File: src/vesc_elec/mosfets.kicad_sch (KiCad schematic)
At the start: 44 parts, among them Q1 NCEP60T20, Q2 NCEP60T20, Q3 NCEP60T20, Q4 NCEP60T20, Q5 NCEP60T20, Q6 NCEP60T20

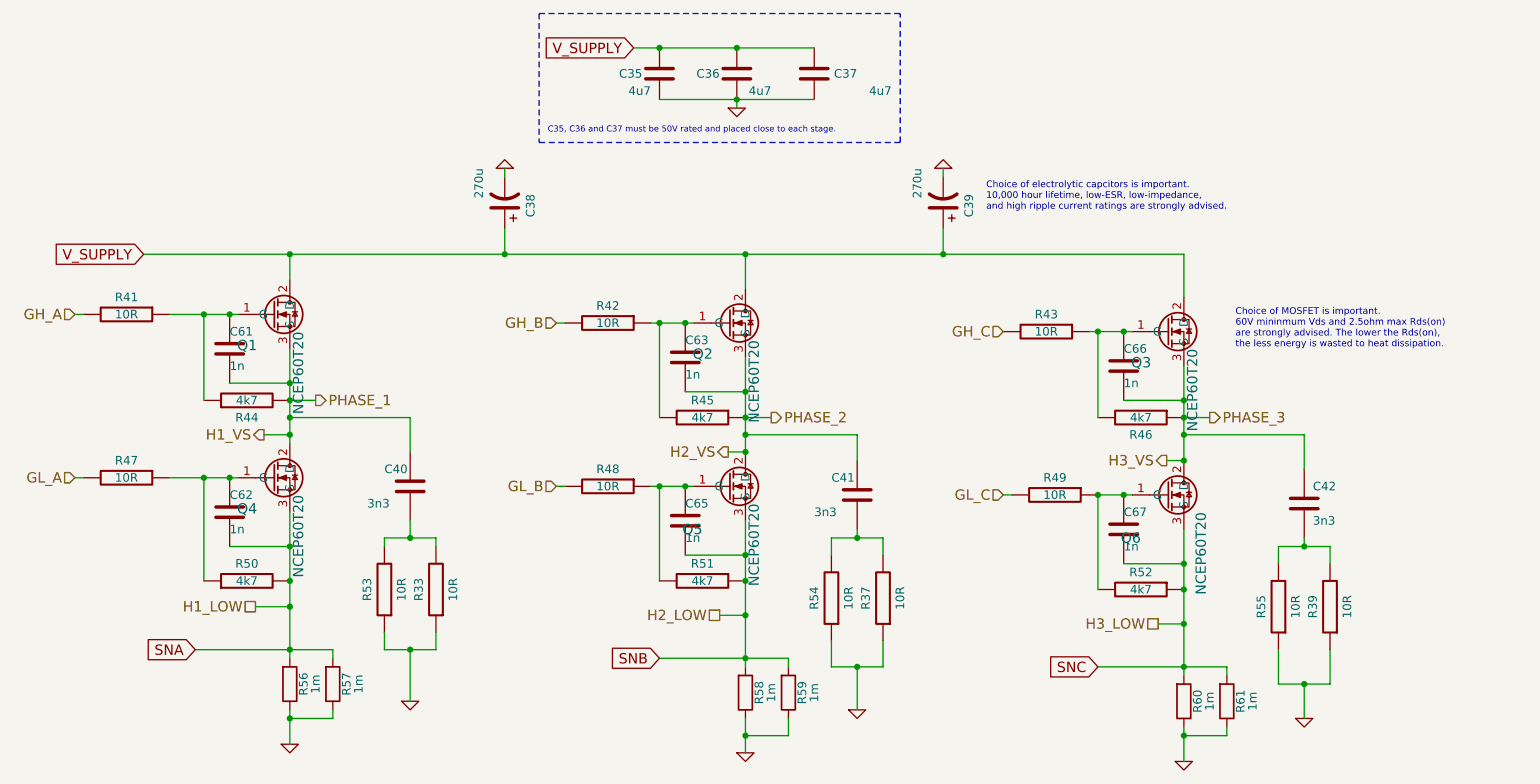
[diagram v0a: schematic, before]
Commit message: [VESC] Swap phase A and C MOSFET labels (#123)
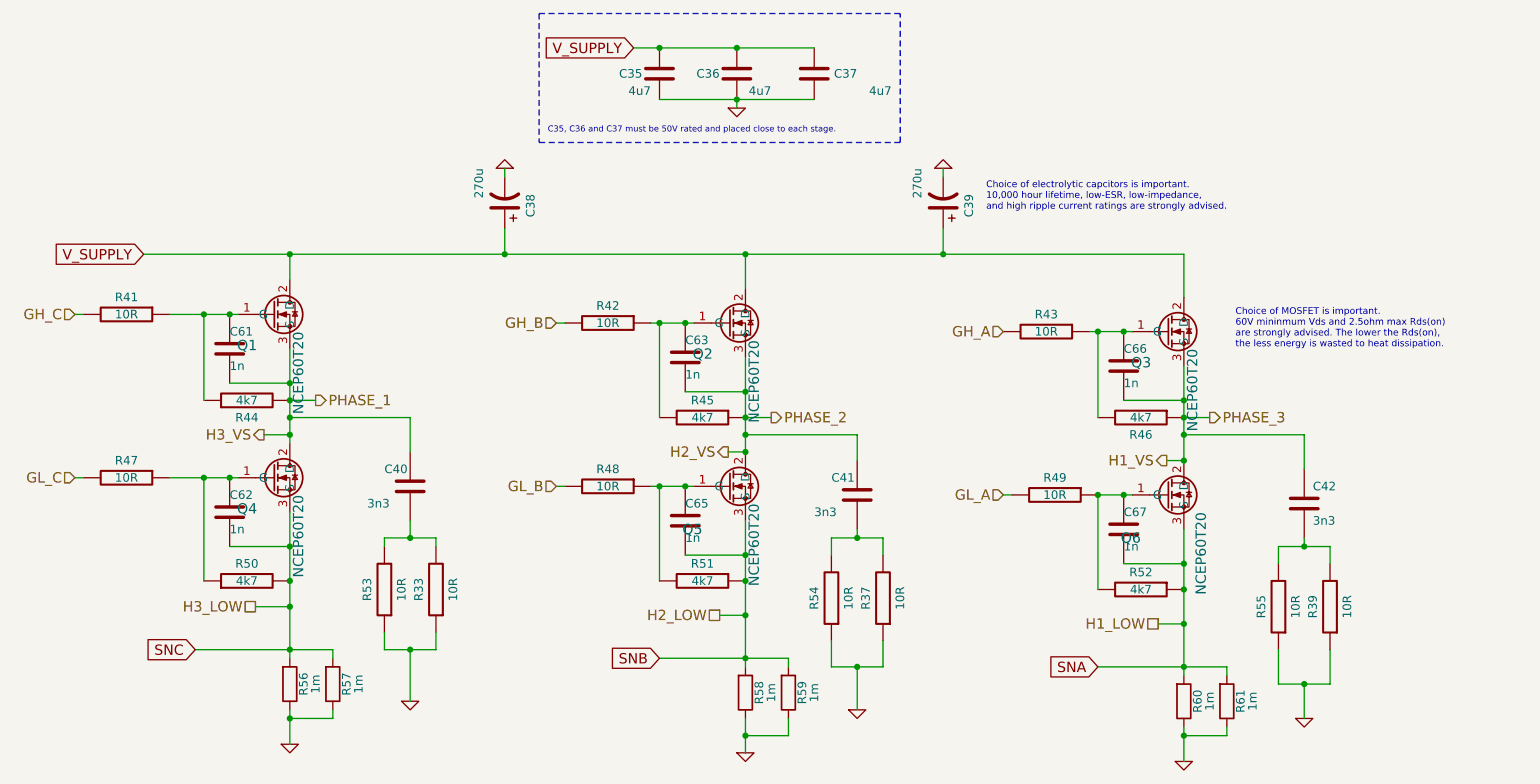
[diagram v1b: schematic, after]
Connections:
- net GH_A: now also R43.2; no longer R41.2
- net GH_C: now also R41.2; no longer R43.2
- net GL_A: now also R49.2; no longer R47.2
- net GL_C: now also R47.2; no longer R49.2
- net H1_VS: now also C42.1, C66.2, Q3.3 (S), Q6.2 (D), Q6.4 (Heatsink), R46.1; no longer C40.1, C61.2, Q1.3 (S), Q4.2 (D), Q4.4 (Heatsink), R44.2
- net H3_VS: now also C40.1, C61.2, Q1.3 (S), Q4.2 (D), Q4.4 (Heatsink), R44.2; no longer C42.1, C66.2, Q3.3 (S), Q6.2 (D), Q6.4 (Heatsink), R46.1
- net SNA: now also C67.2, Q6.3 (S), R52.1, R60.2, R61.2; no longer C62.2, Q4.3 (S), R50.2, R56.2, R57.2
- net SNC: now also C62.2, Q4.3 (S), R50.2, R56.2, R57.2; no longer C67.2, Q6.3 (S), R52.1, R60.2, R61.2
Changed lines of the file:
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@@
+		)
+	)
+	(global_label "SNC"
+		(shape input)
+		(at 81.28 129.54 180)
+		(effects
+			(font
+				(size 1.524 1.524)
+			)
+			(justify right)
+		)
+		(property "Intersheetrefs" "${INTERSHEET_REFS}"
+			(at 81.28 129.54 0)
+			(effects
+				(font
+					(size 1.27 1.27)
+				)
+				(hide yes)
+			)
+		)
+	)
+	(global_label "SNB"
+		(shape input)
+		(at 149.86 130.81 180)
+		(effects
+			(font
+				(size 1.524 1.524)
+			)
+			(justify right)
+		)
+		(property "Intersheetrefs" "${INTERSHEET_REFS}"
+			(at 149.86 130.81 0)
+			(effects
+				(font
+					(size 1.27 1.27)
+				)
+				(hide yes)
+			)
+		)
+	)
+	(global_label "V_SUPPLY"
+		(shape input)
+		(at 146.05 40.64 180)
+		(effects
+			(font
+				(size 1.524 1.524)
+			)
+			(justify right)
+		)
+		(property "Intersheetrefs" "${INTERSHEET_REFS}"
+			(at 146.05 40.64 0)
+			(effects
+				(font
+					(size 1.27 1.27)
+				)
+				(hide yes)
+			)
 		)
 	)
 	(global_label "SNA"
 		(shape input)
-		(at 81.28 129.54 180)
-		(effects
-			(font
-				(size 1.524 1.524)
-			)
-			(justify right)
-		)
-		(property "Intersheetrefs" "${INTERSHEET_REFS}"
-			(at 81.28 129.54 0)
-			(effects
-				(font
-					(size 1.27 1.27)
-				)
-				(hide yes)
-			)
-		)
-	)
-	(global_label "SNB"
-		(shape input)
-		(at 149.86 130.81 180)
-		(effects
-			(font
-				(size 1.524 1.524)
-			)
-			(justify right)
-		)
-		(property "Intersheetrefs" "${INTERSHEET_REFS}"
-			(at 149.86 130.81 0)
+		(at 214.63 132.08 180)
+		(effects
+			(font
+				(size 1.524 1.524)
+			)
+			(justify right)
+		)
+		(property "Intersheetrefs" "${INTERSHEET_REFS}"
+			(at 214.63 132.08 0)
 			(effects
 				(font
@@
 	(global_label "V_SUPPLY"
 		(shape input)
-		(at 146.05 40.64 180)
-		(effects
-			(font
-				(size 1.524 1.524)
-			)
-			(justify right)
-		)
-		(property "Intersheetrefs" "${INTERSHEET_REFS}"
-			(at 146.05 40.64 0)
-			(effects
-				(font
-					(size 1.27 1.27)
-				)
-				(hide yes)
-			)
-		)
-	)
-	(global_label "SNC"
-		(shape input)
-		(at 214.63 132.08 180)
-		(effects
-			(font
-				(size 1.524 1.524)
-			)
-			(justify right)
-		)
-		(property "Intersheetrefs" "${INTERSHEET_REFS}"
-			(at 214.63 132.08 0)
-			(effects
-				(font
-					(size 1.27 1.27)
-				)
-				(hide yes)
-			)
-		)
-	)
-	(global_label "V_SUPPLY"
-		(shape input)
 		(at 73.66 71.12 180)
 		(effects
@@
 			)
 			(justify left)
+		)
+	)
+	(hierarchical_label "H1_LOW"
+		(shape passive)
+		(at 223.52 125.73 180)
+		(effects
+			(font
+				(size 1.524 1.524)
+			)
+			(justify right)
+		)
+	)
+	(hierarchical_label "GH_C"
+		(shape input)
+		(at 63.5 80.01 180)
+		(effects
+			(font
+				(size 1.524 1.524)
+			)
+			(justify right)
+		)
+	)
+	(hierarchical_label "H2_VS"
+		(shape output)
+		(at 160.02 100.33 180)
+		(effects
+			(font
+				(size 1.524 1.524)
+			)
+			(justify right)
+		)
+	)
+	(hierarchical_label "GL_C"
+		(shape input)
+		(at 63.5 104.14 180)
+		(effects
+			(font
+				(size 1.524 1.524)
+			)
+			(justify right)
 		)
 	)
 	(hierarchical_label "H3_LOW"
 		(shape passive)
-		(at 223.52 125.73 180)
+		(at 90.17 123.19 180)
+		(effects
+			(font
+				(size 1.524 1.524)
+			)
+			(justify right)
+		)
+	)
+	(hierarchical_label "GH_B"
+		(shape input)
+		(at 134.62 81.28 180)
+		(effects
+			(font
+				(size 1.524 1.524)
+			)
+			(justify right)
+		)
+	)
+	(hierarchical_label "GL_A"
+		(shape input)
+		(at 200.66 106.68 180)
+		(effects
+			(font
+				(size 1.524 1.524)
+			)
+			(justify right)
+		)
+	)
+	(hierarchical_label "GL_B"
+		(shape input)
+		(at 134.62 105.41 180)
+		(effects
+			(font
+				(size 1.524 1.524)
+			)
+			(justify right)
+		)
+	)
+	(hierarchical_label "H3_VS"
+		(shape output)
+		(at 91.44 97.79 180)
+		(effects
+			(font
+				(size 1.524 1.524)
+			)
+			(justify right)
+		)
+	)
+	(hierarchical_label "H1_VS"
+		(shape output)
+		(at 224.79 101.6 180)
 		(effects
 			(font
@@
 	(hierarchical_label "GH_A"
 		(shape input)
-		(at 63.5 80.01 180)
-		(effects
-			(font
-				(size 1.524 1.524)
-			)
-			(justify right)
-		)
-	)
-	(hierarchical_label "H2_VS"
-		(shape output)
-		(at 160.02 100.33 180)
-		(effects
-			(font
-				(size 1.524 1.524)
-			)
-			(justify right)
-		)
-	)
-	(hierarchical_label "GL_A"
-		(shape input)
-		(at 63.5 104.14 180)
-		(effects
-			(font
-				(size 1.524 1.524)
-			)
-			(justify right)
-		)
-	)
-	(hierarchical_label "H1_LOW"
-		(shape passive)
-		(at 90.17 123.19 180)
-		(effects
-			(font
-				(size 1.524 1.524)
-			)
-			(justify right)
-		)
-	)
-	(hierarchical_label "GH_B"
-		(shape input)
-		(at 134.62 81.28 180)
-		(effects
-			(font
-				(size 1.524 1.524)
-			)
-			(justify right)
-		)
-	)
-	(hierarchical_label "GL_C"
-		(shape input)
-		(at 200.66 106.68 180)
-		(effects
-			(font
-				(size 1.524 1.524)
-			)
-			(justify right)
-		)
-	)
-	(hierarchical_label "GL_B"
-		(shape input)
-		(at 134.62 105.41 180)
-		(effects
-			(font
-				(size 1.524 1.524)
-			)
-			(justify right)
-		)
-	)
-	(hierarchical_label "H1_VS"
-		(shape output)
-		(at 91.44 97.79 180)
-		(effects
-			(font
-				(size 1.524 1.524)
-			)
-			(justify right)
-		)
-	)
-	(hierarchical_label "H3_VS"
-		(shape output)
-		(at 224.79 101.6 180)
-		(effects
-			(font
-				(size 1.524 1.524)
-			)
-			(justify right)
-		)
-	)
-	(hierarchical_label "GH_C"
-		(shape input)
 		(at 200.66 82.55 180)
